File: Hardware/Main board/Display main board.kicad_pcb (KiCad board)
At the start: 2 copper layers, 142.2 x 91.4 mm, 62 parts, among them J1 Board to Board, J3 Conn_01x03, P1 USB_C_Plug_USB2.0, U1 BQ25895RTW, U10 W25Q32JVSS, U2 ABM8-272-T3, U4 RP2040, U5 AP7361C-33E, U6 AP7361C-33E, U7 AP7361C-33E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

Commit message: physical changes
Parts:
- moved J3 1.32 mm to (83.2, 128.3)
- moved P1 0.29 mm to (137.2, 54.6)
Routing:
- net GND: track 275.6 -> 278.9 mm
- net /BMS/NTC: track 25.4 -> 28.4 mm
- net /BMS/BATT+: track 20.0 -> 21.3 mm
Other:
- outline, holes or cut-outs redrawn
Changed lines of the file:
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@@
 	(footprint "Connector_JST:JST_XH_S3B-XH-SM4-TB_1x03-1MP_P2.50mm_Horizontal"
 		(layer "F.Cu")
-		(at 83.2 126.9492 180)
+		(at 83.2 128.27 180)
 		(descr "JST XH series connector, S3B-XH-SM4-TB (http://www.jst-mfg.com/product/pdf/eng/eXH.pdf), generated with kicad-footprint-generator")
 		(tags "connector JST XH horizontal")
@@
 	(footprint "Connector_USB:USB_C_Receptacle_HRO_TYPE-C-31-M-12"
 		(layer "F.Cu")
-		(at 137.16 54.898 180)
+		(at 137.16 54.61 180)
 		(descr "USB Type-C receptacle for USB 2.0 and PD, http://www.krhro.com/uploads/soft/180320/1-1P320120243.pdf")
 		(tags "usb usb-c 2.0 pd")
@@
 		(layer "Edge.Cuts")
 	)
-	(gr_line
-		(start 130.81 50.8)
-		(end 130.81 50.8)
+	(gr_arc
+		(start 208.28 132.08)
+		(mid 205.304205 139.264205)
+		(end 198.12 142.24)
+		(locked yes)
 		(stroke
 			(width 0.1)
@@
 	)
 	(gr_arc
-		(start 208.28 132.08)
-		(mid 205.304205 139.264205)
-		(end 198.12 142.24)
-		(locked yes)
+		(start 142.24 52.07)
+		(mid 142.611974 51.171974)
+		(end 143.51 50.8)
 		(stroke
 			(width 0.1)
@@
 		(layer "Edge.Cuts")
 	)
+	(gr_line
+		(start 143.51 50.8)
+		(end 198.12 50.8)
+		(stroke
+			(width 0.1)
+			(type default)
+		)
+		(layer "Edge.Cuts")
+	)
 	(gr_arc
 		(start 66.04 60.96)
@@
 	)
 	(gr_line
-		(start 198.12 142.24)
-		(end 76.2 142.24)
-		(locked yes)
+		(start 130.81 50.8)
+		(end 76.2 50.8)
 		(stroke
 			(width 0.1)
@@
 	)
 	(gr_line
-		(start 76.2 50.8)
-		(end 198.12 50.8)
+		(start 198.12 142.24)
+		(end 76.2 142.24)
 		(locked yes)
 		(stroke
@@
 		(layer "Edge.Cuts")
 	)
+	(gr_line
+		(start 132.08 52.07)
+		(end 142.24 52.07)
+		(stroke
+			(width 0.1)
+			(type default)
+		)
+		(layer "Edge.Cuts")
+	)
+	(gr_arc
+		(start 130.81 50.8)
+		(mid 131.708026 51.171974)
+		(end 132.08 52.07)
+		(stroke
+			(width 0.1)
+			(type default)
+		)
+		(layer "Edge.Cuts")
+	)
 	(gr_text "+3V3-2\n+VBATT\nMB_CLK\nMB_SCL\nGND"
 		(at 198.755 91.44 90)
@@
 	)
 	(via
-		(at 77.5 121.672)
+		(at 77.5 124.72)
 		(size 0.6)
 		(drill 0.3)
@@
 	)
 	(via
-		(at 77.47 125.0188)
+		(at 88.9 123.19)
 		(size 0.6)
 		(drill 0.3)
@@
 	)
 	(via
-		(at 88.9 123.19)
+		(at 88.893119 126.273706)
 		(size 0.6)
 		(drill 0.3)
@@
 	)
 	(via
-		(at 88.9 125.0696)
+		(at 88.9 124.72)
 		(size 0.6)
 		(drill 0.3)
@@
 	)
 	(via
-		(at 88.9 121.672)
+		(at 77.461892 126.305284)
 		(size 0.6)
 		(drill 0.3)
@@
 	)
 	(segment
+		(start 92.583 118.491)
+		(end 92.583 133.477)
+		(width 0.8)
+		(layer "F.Cu")
+		(net 5)
+	)
+	(segment
 		(start 84.455 73.634)
 		(end 85.318 72.771)
@@
 	)
 	(segment
-		(start 92.583 118.491)
-		(end 92.583 131.953)
-		(width 0.8)
-		(layer "F.Cu")
-		(net 5)
-	)
-	(segment
 		(start 78.2066 109.1398)
 		(end 78.2066 108.6866)
@@
 	)
 	(segment
-		(start 80.7 132.262)
-		(end 80.7 130.1992)
-		(width 0.8)
-		(layer "F.Cu")
-		(net 5)
-	)
-	(segment
 		(start 84.225 114.046)
 		(end 84.225 113.9789)
@@
 	)
 	(segment
+		(start 82.55 135.89)
+		(end 80.7 134.04)
+		(width 0.8)
+		(layer "F.Cu")
+		(net 5)
+	)
+	(segment
 		(start 166.37 66.548)
 		(end 166.3446 66.5226)
@@
 	)
 	(segment
+		(start 80.7 134.04)
+		(end 80.7 131.52)
+		(width 0.8)
+		(layer "F.Cu")
+		(net 5)
+	)
+	(segment
 		(start 133.91 58.943)
 		(end 133.5278 58.5608)
@@
 	)
 	(segment
+		(start 79.1334 118.3132)
+		(end 79.1334 123.177)
+		(width 0.8)
+		(layer "F.Cu")
+		(net 5)
+	)
+	(segment
 		(start 76.5556 107.7976)
 		(end 76.5556 108.2548)
@@
 	)
 	(segment
-		(start 79.1334 123.177)
-		(end 80.7 124.7436)
-		(width 0.8)
-		(layer "F.Cu")
-		(net 5)
-	)
-	(segment
 		(start 195.785 73.357)
 		(end 196.067 73.639)
@@
 	)
 	(segment
-		(start 80.7 124.7436)
-		(end 80.7 130.1992)
-		(width 0.8)
-		(layer "F.Cu")
-		(net 5)
-	)
-	(segment
 		(start 140.41 58.943)
 		(end 140.565 58.943)
@@
 	)
 	(segment
-		(start 195.785 72.107)
-		(end 195.785 73.357)
-		(width 0.2)
+		(start 90.17 135.89)
+		(end 82.55 135.89)
+		(width 0.8)
 		(layer "F.Cu")
 		(net 5)
 	)
 	(segment
-		(start 92.583 131.953)
-		(end 90.2716 134.2644)
+		(start 92.583 133.477)
+		(end 90.17 135.89)
 		(width 0.8)
 		(layer "F.Cu")
@@
 	)
 	(segment
+		(start 195.785 72.107)
+		(end 195.785 73.357)
+		(width 0.2)
+		(layer "F.Cu")
+		(net 5)
+	)
+	(segment
 		(start 88.3412 102.7554)
 		(end 88.3412 102.0826)
@@
 	)
 	(segment
-		(start 79.1334 118.3132)
-		(end 79.1334 123.177)
-		(width 0.8)
-		(layer "F.Cu")
-		(net 5)
-	)
-	(segment
-		(start 90.2716 134.2644)
-		(end 82.7024 134.2644)
-		(width 0.8)
-		(layer "F.Cu")
-		(net 5)
-	)
-	(segment
 		(start 85.5472 116.2812)
 		(end 84.225 114.959)
@@
 	)
 	(segment
+		(start 79.1334 123.177)
+		(end 80.7 124.7436)
+		(width 0.8)
+		(layer "F.Cu")
+		(net 5)
+	)
+	(segment
 		(start 84.72 65.4922)
 		(end 84.5532 65.659)
@@
 	)
 	(segment
-		(start 82.7024 134.2644)
-		(end 80.7 132.262)
+		(start 80.7 124.7436)
+		(end 80.7 131.52)
 		(width 0.8)
 		(layer "F.Cu")
@@
 	)
 	(via
-		(at 80.7 128.472)
+		(at 80.7 131.52)
 		(size 0.6)
 		(drill 0.3)
@@
 	)
 	(segment
-		(start 85.7 130.1992)
+		(start 83.922 121.158)
 		(end 85.7 122.936)
 		(width 0.8)
@@
 	)
 	(segment
-		(start 83.922 121.158)
-		(end 85.7 122.936)
+		(start 82.169 121.158)
+		(end 83.922 121.158)
 		(width 0.8)
 		(layer "F.Cu")
@@
 	)
 	(segment
-		(start 82.169 121.158)
-		(end 83.922 121.158)
+		(start 85.7 131.52)
+		(end 85.7 122.936)
 		(width 0.8)
 		(layer "F.Cu")
@@
 	)
 	(via
-		(at 85.7 128.472)
+		(at 85.7 131.52)
 		(size 0.6)
 		(drill 0.3)
@@
 	)
 	(via
-		(at 83.2 128.472)
+		(at 83.2 131.52)
 		(size 0.6)
 		(drill 0.3)
@@
 	(segment
 		(start 83.2 119.0752)
-		(end 83.2 128.472)
+		(end 83.2 131.52)
 		(width 0.2)
 		(layer "B.Cu")

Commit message: Part selection
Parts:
- R8: value 260 -> 260Ω; footprint Resistor_SMD:R_0402_1005Metric -> Resistor_SMD:R_0603_1608Metric
- U3: value ~ -> TS3USB221A
- moved R8 0.43 mm to (78.2, 109.2)

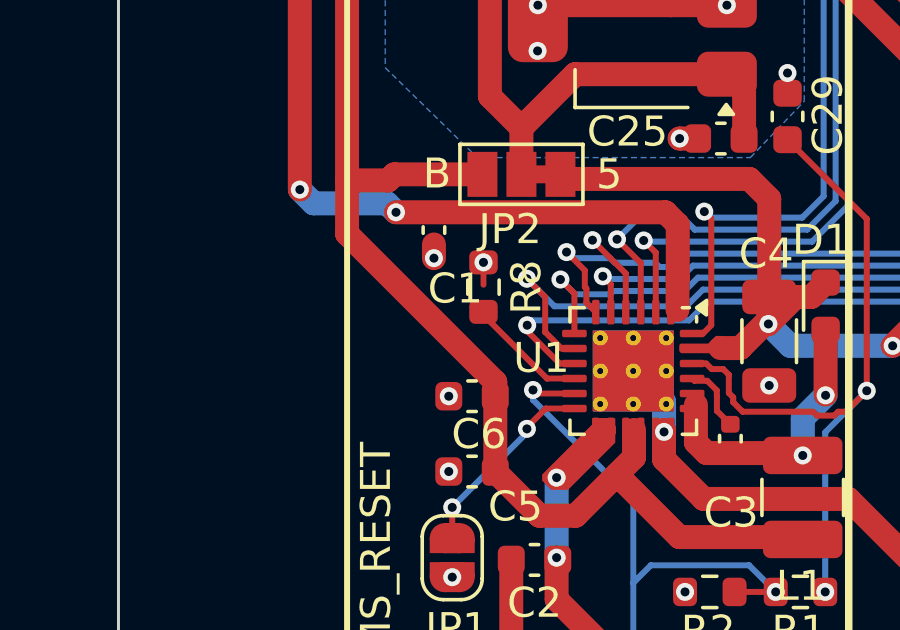
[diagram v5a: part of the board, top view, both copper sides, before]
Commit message: Swap 260Ω footprint for 0805
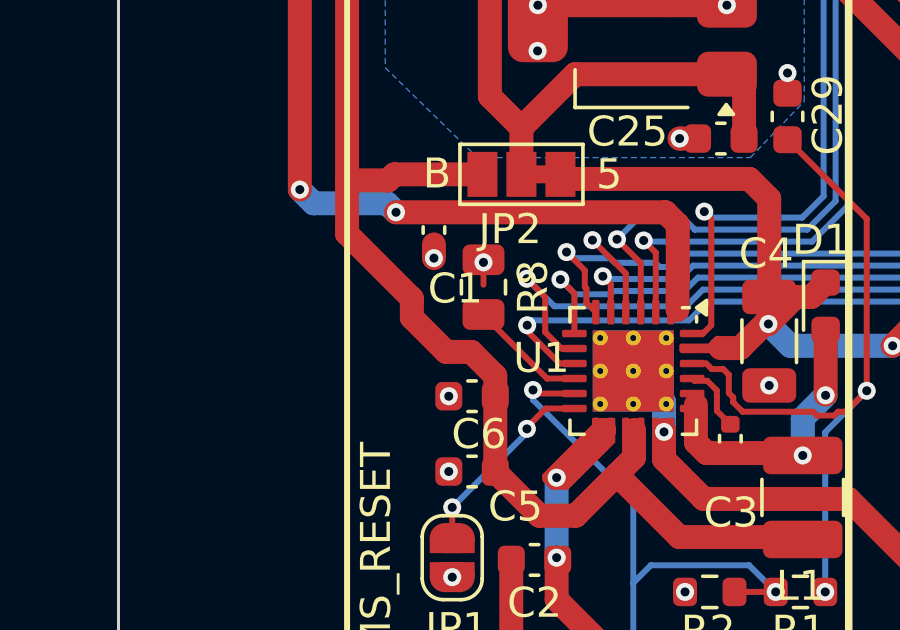
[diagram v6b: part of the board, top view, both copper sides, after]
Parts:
- R8: footprint Resistor_SMD:R_0603_1608Metric -> Resistor_SMD:R_0805_2012Metric
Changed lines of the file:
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@@
 		)
 	)
-	(footprint "Resistor_SMD:R_0603_1608Metric"
+	(footprint "Resistor_SMD:R_0805_2012Metric"
 		(layer "F.Cu")
 		(at 78.2066 109.22 -90)
-		(descr "Resistor SMD 0603 (1608 Metric), square (rectangular) end terminal, IPC_7351 nominal, (Body size source: IPC-SM-782 page 72, https://www.pcb-3d.com/wordpress/wp-content/uploads/ipc-sm-782a_amendment_1_and_2.pdf), generated with kicad-footprint-generator")
+		(descr "Resistor SMD 0805 (2012 Metric), square (rectangular) end terminal, IPC_7351 nominal, (Body size source: IPC-SM-782 page 72, https://www.pcb-3d.com/wordpress/wp-content/uploads/ipc-sm-782a_amendment_1_and_2.pdf), generated with kicad-footprint-generator")
 		(tags "resistor")
 		(property "Reference" "R8"
-			(at 0 -1.43 -90)
+			(at 0 -1.65 -90)
 			(layer "F.SilkS")
 			(effects
@@
 		)
 		(property "Value" "260Ω"
-			(at 0 1.43 -90)
+			(at 0 1.65 -90)
 			(layer "F.Fab")
 			(effects
@@
 			)
 		)
-		(property "Footprint" "Resistor_SMD:R_0603_1608Metric"
+		(property "Footprint" "Resistor_SMD:R_0805_2012Metric"
 			(at 0 0 -90)
 			(unlocked yes)
@@
 		(attr smd)
 		(fp_line
-			(start -0.237258 0.5225)
-			(end 0.237258 0.5225)
+			(start -0.227064 0.735)
+			(end 0.227064 0.735)
 			(stroke
 				(width 0.12)
@@
 		)
 		(fp_line
-			(start -0.237258 -0.5225)
-			(end 0.237258 -0.5225)
+			(start -0.227064 -0.735)
+			(end 0.227064 -0.735)
 			(stroke
 				(width 0.12)
@@
 		)
 		(fp_line
-			(start -1.48 0.73)
-			(end -1.48 -0.73)
+			(start -1.68 0.95)
+			(end -1.68 -0.95)
 			(stroke
 				(width 0.05)
@@
 		)
 		(fp_line
-			(start 1.48 0.73)
-			(end -1.48 0.73)
+			(start 1.68 0.95)
+			(end -1.68 0.95)
 			(stroke
 				(width 0.05)
@@
 		)
 		(fp_line
-			(start -1.48 -0.73)
-			(end 1.48 -0.73)
+			(start -1.68 -0.95)
+			(end 1.68 -0.95)
 			(stroke
 				(width 0.05)
@@
 		)
 		(fp_line
-			(start 1.48 -0.73)
-			(end 1.48 0.73)
+			(start 1.68 -0.95)
+			(end 1.68 0.95)
 			(stroke
 				(width 0.05)
@@
 		)
 		(fp_line
-			(start -0.8 0.4125)
-			(end -0.8 -0.4125)
+			(start -1 0.625)
+			(end -1 -0.625)
 			(stroke
 				(width 0.1)
@@
 		)
 		(fp_line
-			(start 0.8 0.4125)
-			(end -0.8 0.4125)
+			(start 1 0.625)
+			(end -1 0.625)
 			(stroke
 				(width 0.1)
@@
 		)
 		(fp_line
-			(start -0.8 -0.4125)
-			(end 0.8 -0.4125)
+			(start -1 -0.625)
+			(end 1 -0.625)
 			(stroke
 				(width 0.1)
@@
 		)
 		(fp_line
-			(start 0.8 -0.4125)
-			(end 0.8 0.4125)
+			(start 1 -0.625)
+			(end 1 0.625)
 			(stroke
 				(width 0.1)
@@
 			(effects
 				(font
-					(size 0.4 0.4)
-					(thickness 0.06)
+					(size 0.5 0.5)
+					(thickness 0.08)
 				)
 			)
 		)
 		(pad "1" smd roundrect
-			(at -0.825 0 270)
-			(size 0.8 0.95)
+			(at -0.9125 0 270)
+			(size 1.025 1.4)
 			(layers "F.Cu" "F.Paste" "F.Mask")
-			(roundrect_rratio 0.25)
+			(roundrect_rratio 0.243902)
 			(net 5 "GND")
 			(pintype "passive")
 		)
 		(pad "2" smd roundrect
-			(at 0.825 0 270)
-			(size 0.8 0.95)
+			(at 0.9125 0 270)
+			(size 1.025 1.4)
 			(layers "F.Cu" "F.Paste" "F.Mask")
-			(roundrect_rratio 0.25)
+			(roundrect_rratio 0.243902)
 			(net 66 "Net-(U1-ILIM)")
 			(pintype "passive")
 		)
-		(model "${KICAD8_3DMODEL_DIR}/Resistor_SMD.3dshapes/R_0603_1608Metric.wrl"
+		(model "${KICAD8_3DMODEL_DIR}/Resistor_SMD.3dshapes/R_0805_2012Metric.wrl"
 			(offset
 				(xyz 0 0 0)
@@
 	)
 	(segment
-		(start 81.28 116.84)
-		(end 82.6516 115.4684)
+		(start 78.6006 112.8568)
+		(end 78.6006 112.1794)
 		(width 0.8)
 		(layer "F.Cu")
@@
 	)
 	(segment
-		(start 78.6006 115.3668)
-		(end 80.0738 116.84)
+		(start 81.28 116.84)
+		(end 82.6516 115.4684)
 		(width 0.8)
 		(layer "F.Cu")
@@
 	)
 	(segment
-		(start 78.6006 112.3818)
-		(end 73.66 107.4412)
+		(start 78.6006 115.3668)
+		(end 80.0738 116.84)
 		(width 0.8)
 		(layer "F.Cu")
@@
 	)
 	(segment
+		(start 75.8194 109.6006)
+		(end 73.66 107.4412)
+		(width 0.8)
+		(layer "F.Cu")
+		(net 9)
+	)
+	(segment
 		(start 81.992428 71.696)
 		(end 73.66 80.028428)
@@
 	)
 	(segment
+		(start 78.6006 112.1794)
+		(end 77.8002 111.379)
+		(width 0.8)
+		(layer "F.Cu")
+		(net 9)
+	)
+	(segment
 		(start 85.777 71.696)
 		(end 81.992428 71.696)
@@
 	)
 	(segment
-		(start 73.66 107.4412)
-		(end 73.66 105.664)
-		(width 0.8)
-		(layer "F.Cu")
-		(net 9)
-	)
-	(segment
 		(start 85.777 71.696)
 		(end 87.44096 71.696)
@@
 	)
 	(segment
-		(start 87.44096 71.696)
-		(end 91.3892 75.64424)
+		(start 75.8194 110.2364)
+		(end 75.8194 109.6006)
 		(width 0.8)
 		(layer "F.Cu")
@@
 	)
 	(segment
-		(start 78.6006 112.8568)
-		(end 78.6006 112.3818)
+		(start 76.962 111.379)
+		(end 75.8194 110.2364)
+		(width 0.8)
+		(layer "F.Cu")
+		(net 9)
+	)
+	(segment
+		(start 73.66 107.4412)
+		(end 73.66 105.664)
+		(width 0.8)
+		(layer "F.Cu")
+		(net 9)
+	)
+	(segment
+		(start 87.44096 71.696)
+		(end 91.3892 75.64424)
 		(width 0.8)
 		(layer "F.Cu")
@@
 		(width 0.8)
 		(layer "F.Cu")
+		(net 9)
+	)
+	(segment
+		(start 77.8002 111.379)
+		(end 76.962 111.379)
+		(width 0.8)
+		(layer "F.Cu")

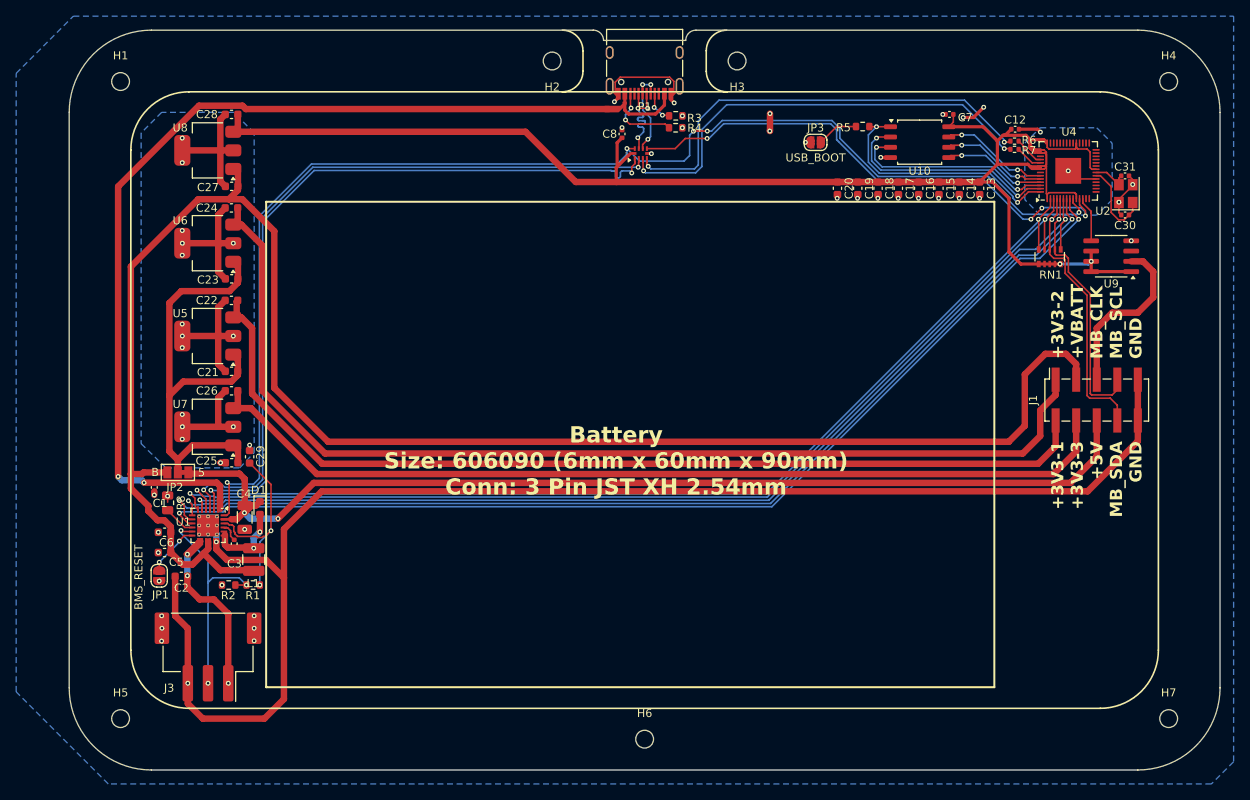
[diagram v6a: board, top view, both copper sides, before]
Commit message: Fix BMS_STAT pin
swapped RP2040 footprint for one with thermal vias
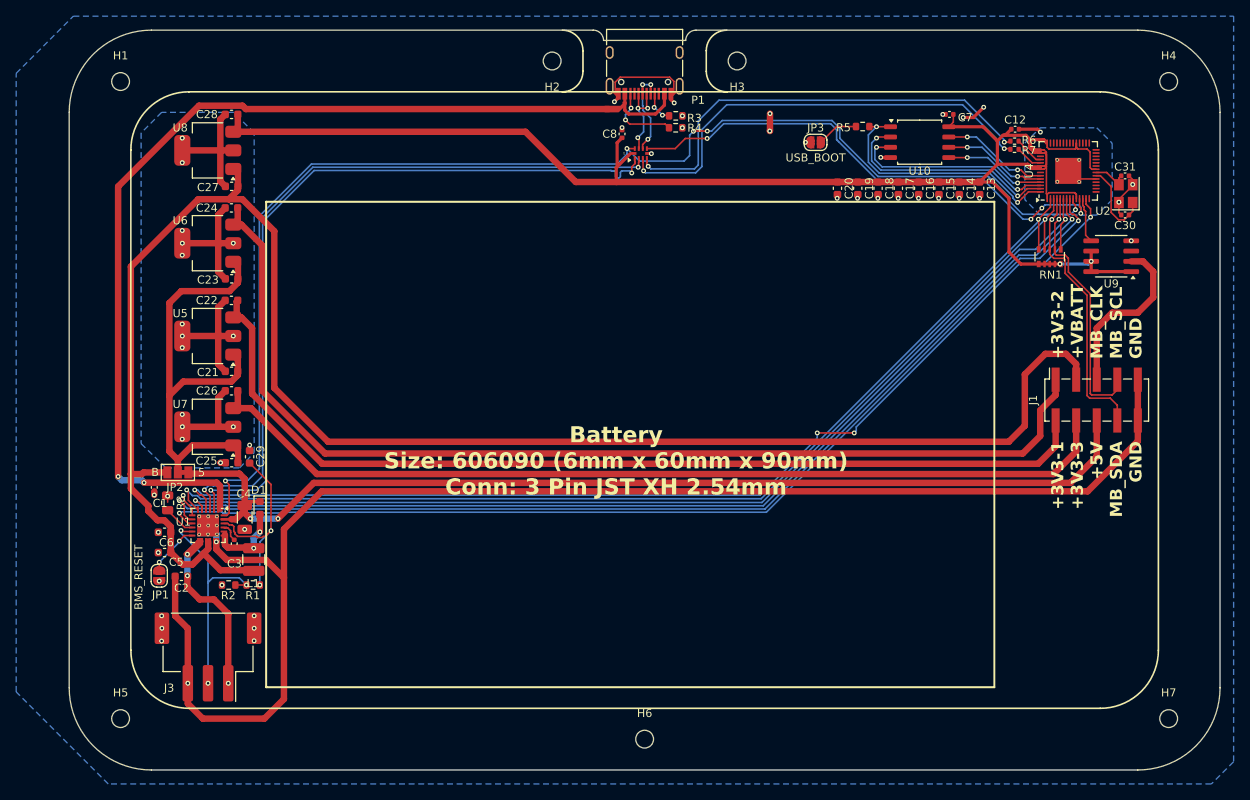
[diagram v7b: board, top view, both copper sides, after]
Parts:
- U4: footprint Package_DFN_QFN:QFN-56-1EP_7x7mm_P0.4mm_EP3.2x3.2mm -> Package_DFN_QFN:QFN-56-1EP_7x7mm_P0.4mm_EP3.2x3.2mm_ThermalVias
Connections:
- U1 pad 4: /BMS/STAT -> /BMS_STAT
- U4 pad 13: unconnected-(U4-GPIO10-Pad13) -> /BMS_STAT
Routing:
- net /BMS_STAT: track 0.00 -> 131.5 mm, vias 0 -> 4
- net /BMS/STAT: track 2.86 -> 0.00 mm, vias 1 -> 0
- net /USB_D+: track 12.7 -> 9.94 mm
- net /BMS_INT: track 131.9 -> 134.1 mm
- net SYS_SDA: track 128.8 -> 130.1 mm
- net /USB_DSEL: track 159.6 -> 158.4 mm
- net SYS_SCL: track 127.0 -> 127.9 mm
- net /USB_DIS: track 64.8 -> 64.0 mm
- net /BMS_D-: track 93.4 -> 92.8 mm
- net +5V: track 130.5 -> 130.0 mm
- net GND: vias 51 -> 50

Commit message: Update GND symbols
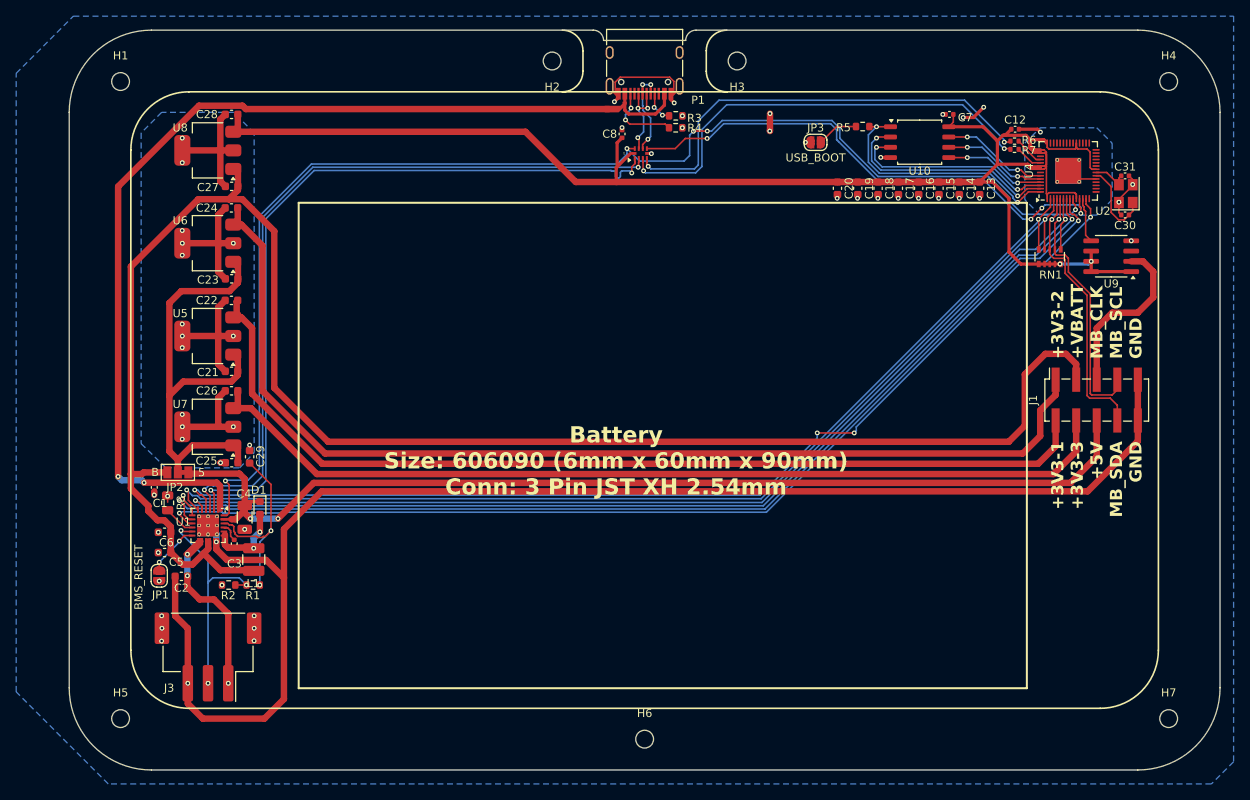
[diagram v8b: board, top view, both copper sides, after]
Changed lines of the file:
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@@
 	)
 	(gr_rect
-		(start 90.382 72.009)
-		(end 180.382 132.009)
+		(start 94.404 72.136)
+		(end 184.404 132.136)
 		(stroke
 			(width 0.25)
@@
 	)
 	(gr_rect
-		(start 90.382 72.136)
-		(end 180.382 132.136)
+		(start 94.404 72.136)
+		(end 184.404 132.136)
 		(stroke
 			(width 0.25)
